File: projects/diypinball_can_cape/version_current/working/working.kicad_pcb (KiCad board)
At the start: 2 copper layers, 86.4 x 54.6 mm, 42 parts, among them P1 BEAGLEBONE_BLACK, P2 PINBALL-CONNECTOR, P3 PINBALL-CONNECTOR, U1 MCP2562, U2 24C256, U3 AP3513E

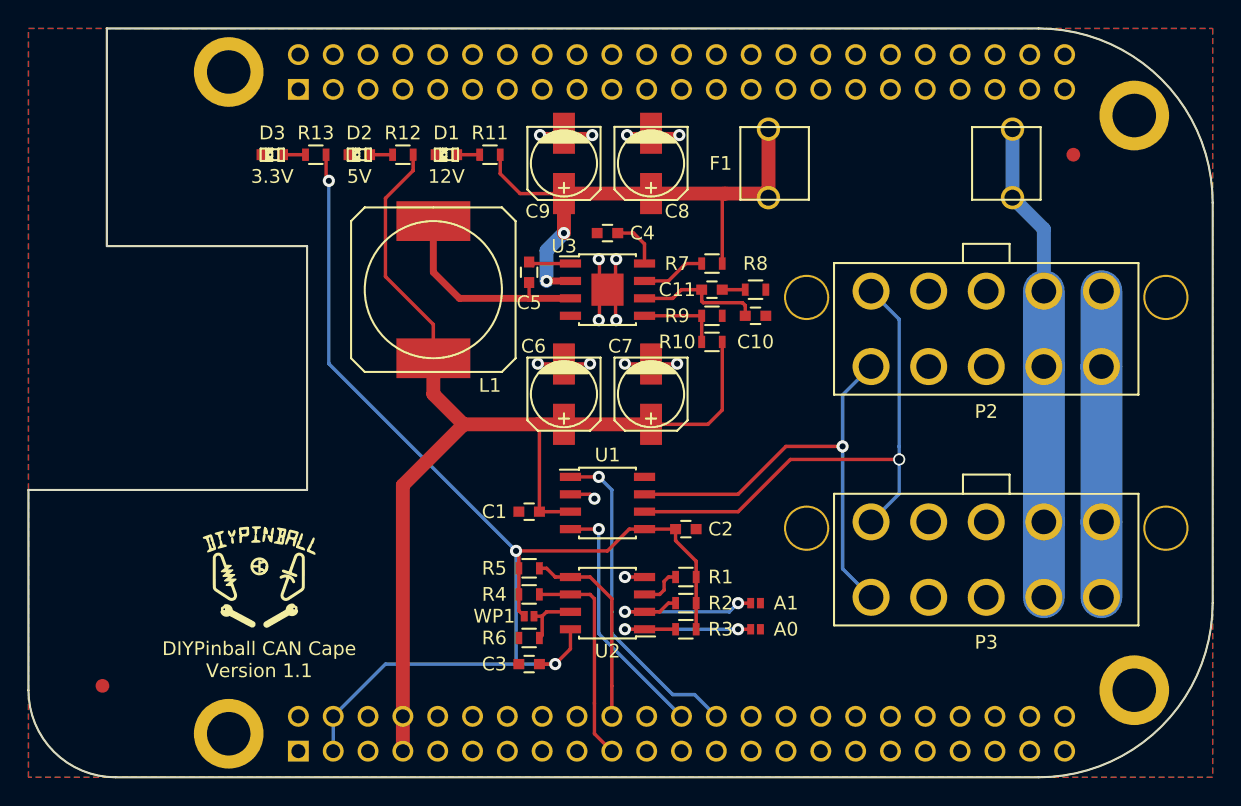
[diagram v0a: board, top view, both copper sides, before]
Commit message: converted omerk brd to kicad
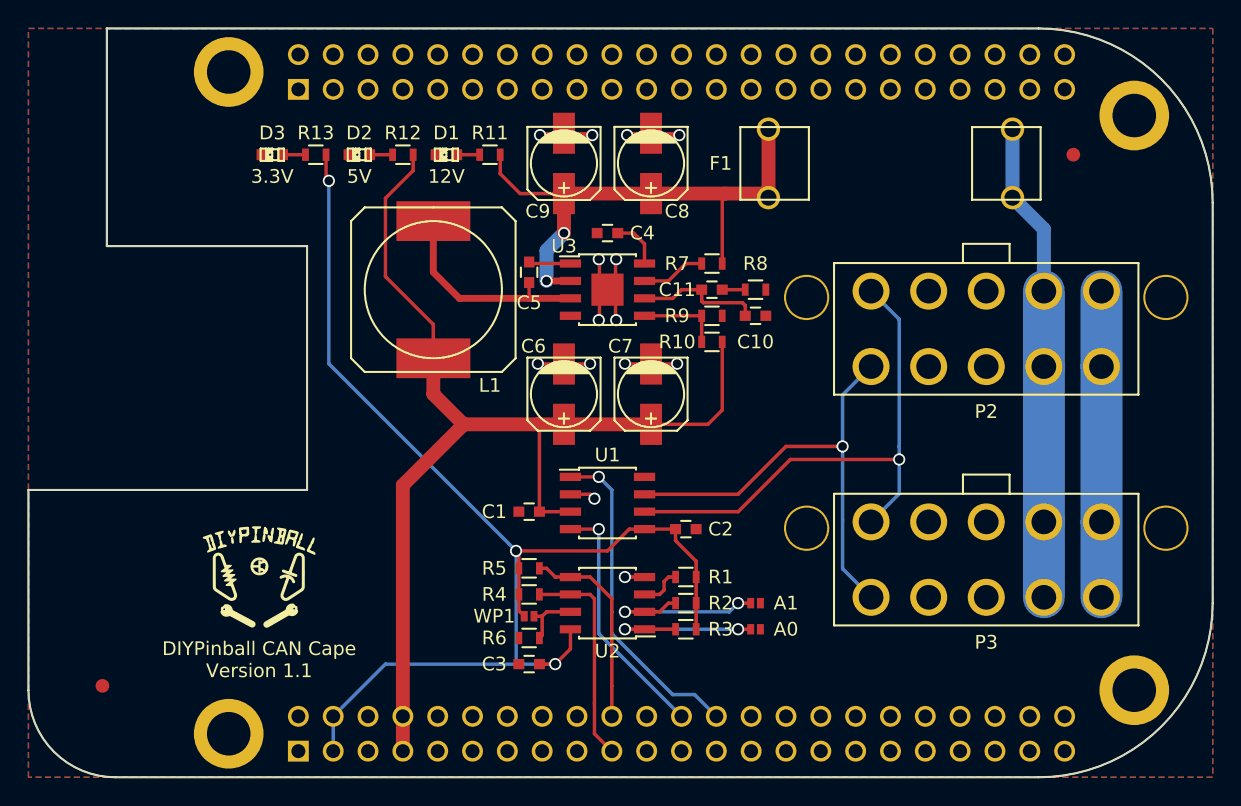
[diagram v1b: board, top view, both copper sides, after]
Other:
- net class Default removed

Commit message: updated all projects from src
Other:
- net class Default added: clearance 0.254, trace_width 0.254, via_dia 0.889, via_drill 0.635
